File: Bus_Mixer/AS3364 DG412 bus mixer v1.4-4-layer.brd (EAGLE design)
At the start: 84.8 x 52.5 mm, 140 parts, among them IC1 PCA9539PW, IC10 DG412-J, IC11 DG412-J, IC2 TL074JT, IC3 TL072JT, IC4 TL074JT, IC6 TL072JT, IC7 TL074JT, IC8 DG412-J, IC9 DG412-J

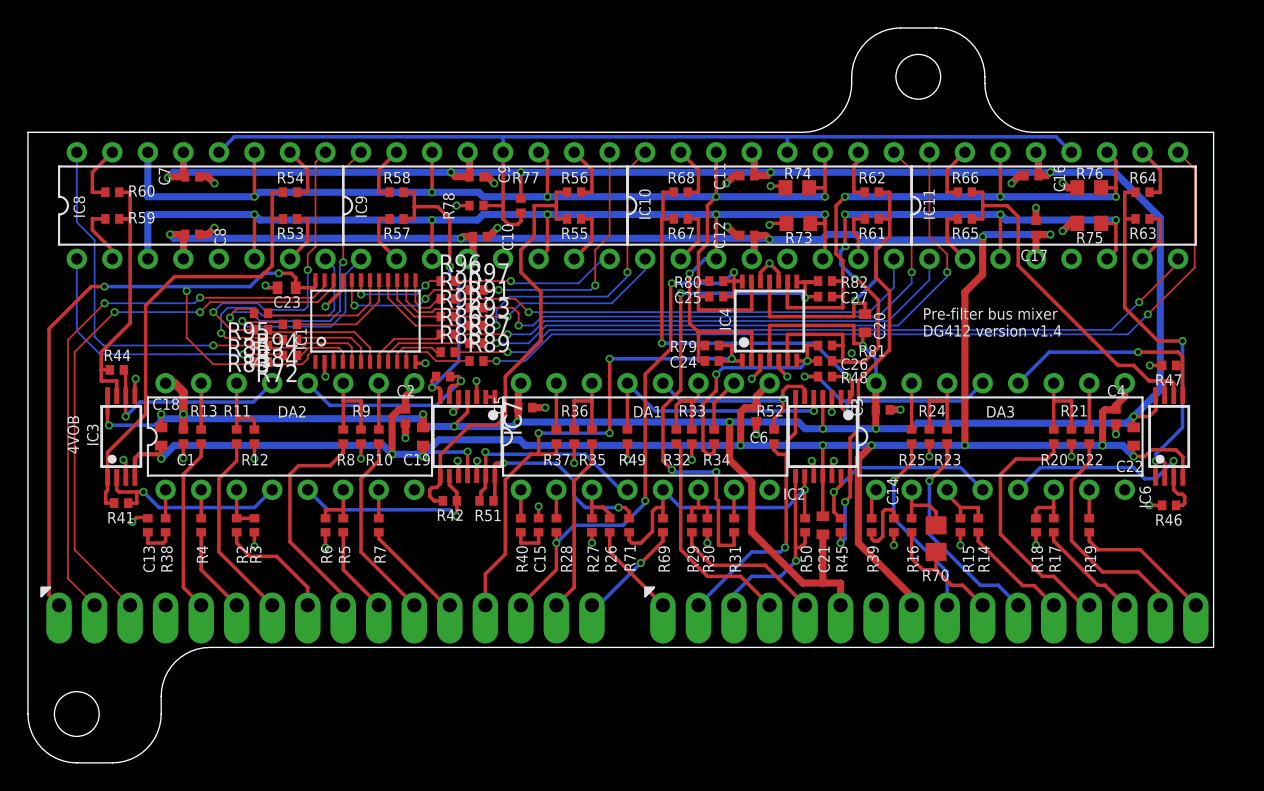
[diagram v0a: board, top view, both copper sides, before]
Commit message: Added better decoupling caps
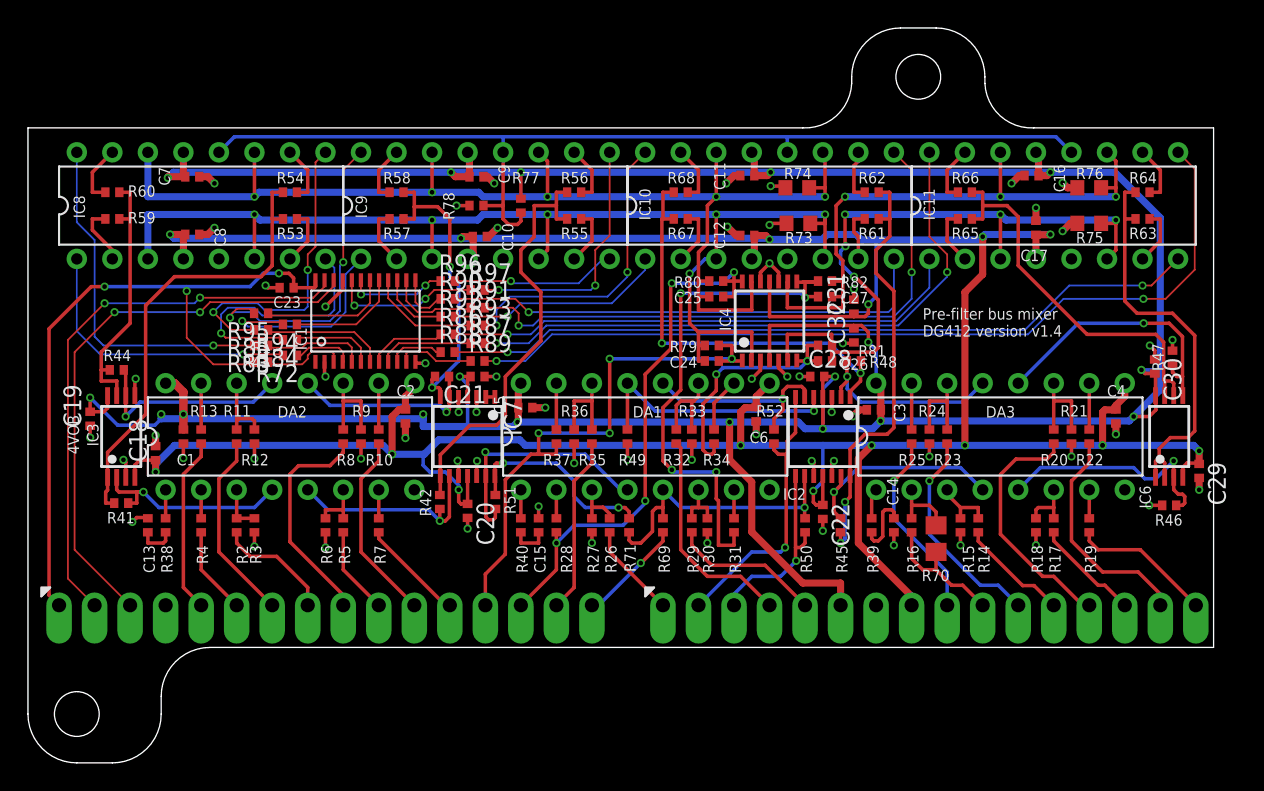
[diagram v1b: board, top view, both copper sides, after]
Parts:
- added C28, C29, C30, C31, C32: 1uF, joakim:C0402-J
- C18, C19, C20, C21, C22, C23: device rcl:C0402 -> joakim:C0402-J
- moved C20 31.4 mm to (30.5, 9.76)
- moved C21 26.9 mm to (31.2, 19.4), turned to 180 degrees
- moved C19 23.8 mm to (3.49, 16.4)
- moved C22 22.9 mm to (55.9, 9.68), turned to 270 degrees
- moved R48 2.34 mm to (58.1, 20.5)
- moved C18 1.26 mm to (8.18, 13.9)
- moved R42 0.72 mm to (28.5, 10.4), turned to 270 degrees
- moved R51 0.64 mm to (32.5, 10.4), turned to 270 degrees
- moved C3 0.63 mm to (59.5, 17.0), turned to 0 degrees
- moved R47 0.60 mm to (80.9, 20.7), turned to 90 degrees
- moved R87 0.08 mm to (31.2, 21.7)
- moved R89 0.08 mm to (31.2, 20.5)
- moved R91 0.08 mm to (31.2, 24.3)
- moved R93 0.08 mm to (31.2, 23.0)
- moved R97 0.08 mm to (31.2, 25.6)
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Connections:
- net +12V: now also C28.2, C30.2, C32.2; no longer C18.2, C20.2, C22.2
- net -12V: now also C29.1, C31.1; no longer C19.1, C21.1
- net GND: now also C18.2, C19.1, C20.2, C21.1, C22.2, C28.1, C29.2, C30.1, C31.2, C32.1
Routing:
- net +12V: track 235.9 -> 245.8 mm, vias 16 -> 18
- net GND: track 60.4 -> 69.1 mm, vias 54 -> 63
- net -12V: track 231.0 -> 234.5 mm, vias 16 -> 15
- net N$19: track 16.1 -> 19.5 mm
- net CON5: track 17.1 -> 14.3 mm, vias 2 -> 1
- net N$17: track 15.0 -> 17.4 mm
- net BUS_FX_A: track 50.3 -> 48.3 mm
- net OUT8: track 27.2 -> 29.0 mm, vias 2 -> 0
- net OUT4: track 32.5 -> 30.8 mm
- net CON3: track 15.0 -> 13.4 mm
- net OUT7: track 26.3 -> 27.9 mm
- net OUT6: track 29.7 -> 30.9 mm
- net OUT5: track 29.4 -> 30.4 mm
- net DIG_6_BUS_A: track 34.6 -> 35.4 mm
- net DIG_6_BUS_B: track 42.8 -> 43.4 mm
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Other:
- outline, holes or cut-outs redrawn
